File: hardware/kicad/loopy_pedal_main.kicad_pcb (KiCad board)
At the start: 2 copper layers, 82 x 94 mm, 84 parts, among them J1 USB, J10 MOCO, J11 IND, J12 UNDO, J13 MODE, J14 TRACK1, J15 TRACK2, J16 TRACK3, J17 TRACK4, J18 CLEAR, J19 BANK, J2 9V, J3 RECPLAY, J4 STOP, J5 RING, J6 ICSP U1, J7 ICSP U2, J8 MIDI OUT, J9 MIDI IN, Q1 AO3401A, SW1 RST U1, SW2 RST U2, U1 ATmega328P-A, U10 74AHCT1G08, U2 ATmega16U2-A, U3 AP63203WU, U4 74AHCT1G125, U5 LM66100DCK, U6 LM66100DCK, U7 USBLC6-2SC6, U8 74AHCT1G125, U9 H11L1, Y1 16MHz, Y2 16MHz

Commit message: fix(pcb): correct reverse-polarity FET, LM66100 footprint, ISP caps, TVS
Fixes all issues found during circuit validation + the assembled-board quote:

- Q1 (reverse-polarity P-FET): swap Source/Drain so Drain=input, Source=load,
  Gate=GND. The body diode now blocks reverse polarity instead of conducting
  it straight to the board. Normal operation unchanged.
- U5/U6 (LM66100 ideal diodes): footprint SOT-23-6 -> SOT-363_SC-70-6 (the
  LM66100DCK is an SC-70-6 part; the old footprint would not have fit).
- CLEAR (PB3/MOSI) + BANK (PB4/MISO) debounce caps: 100nF -> 1nF so the shared
  ICSP lines stay clean for in-system programming (firmware debounces anyway).
- D1: value TVS_SMBJ12A -> SMAJ12A to match the D_SMA footprint + the BOM part
  (Littelfuse SMAJ12A, 400W, C148213).

Rebuilt netlist -> board -> place -> route -> DRC: 969 segments, 67 vias,
2 GND pours, DRC 0 errors / 0 unconnected / 0 silk warnings.

Regenerated fab package (gerbers+drill, CPL, BOM) and JLCPCB upload files;
all 26 SMT BOM lines carry an in-stock LCSC part (new 1nF = C1588).

Co-Authored-By: Claude Opus 4.8 <noreply@anthropic.com>
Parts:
- C17, C18: value 100nF -> 1nF
- D1: value TVS_SMBJ12A -> SMAJ12A
- U5, U6: footprint SOT-23-6 -> SOT-363_SC-70-6
- moved C7 41.3 mm to (77.7, 92.8)
- moved C20 35.0 mm to (70.9, 96.9)
- moved C19 31.3 mm to (40.4, 90.1)
- moved C6 22.5 mm to (102.4, 81.4)
- moved C12 15.4 mm to (92.9, 95.4)
- moved C9 11.9 mm to (92.9, 97.8)
- moved U5 11.4 mm to (42.0, 84.9)
- moved C27 11.0 mm to (37.3, 85.0)
- moved Q1 9.98 mm to (37.0, 81.2)
- moved U6 9.43 mm to (45.8, 84.9)
- moved C25 9.34 mm to (49.6, 84.5)
- moved U4 9.03 mm to (50.0, 76.8)
- moved C8 8.77 mm to (85.2, 95.4)
- moved C15 8.21 mm to (85.2, 100.1)
- moved R14 8.21 mm to (48.1, 87.7)
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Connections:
- Q1 pad 2: VIN_RAW -> +9V
- Q1 pad 3: +9V -> VIN_RAW
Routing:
- net RING_DATA: track 53.9 -> 100.8 mm, vias 2 -> 0
- net GND: track 571.3 -> 607.2 mm, vias 4 -> 1
- net FB: track 49.4 -> 16.1 mm, vias 0 -> 2
- net N$16: track 37.4 -> 10.0 mm
- net SW_NODE: track 52.4 -> 26.5 mm, vias 0 -> 2
- net IND_DATA: track 62.8 -> 87.7 mm, vias 2 -> 0
- net N$21: track 71.0 -> 94.0 mm
- net SW_RECPLAY: track 77.7 -> 97.8 mm, vias 3 -> 2
- net +5V: track 250.0 -> 230.1 mm, vias 5 -> 9
- net SW_STOP: track 89.7 -> 70.3 mm
- net RST_16: track 40.5 -> 58.3 mm, vias 0 -> 1
- net RST_328: track 67.5 -> 51.3 mm
- net SW_MODE: track 60.0 -> 74.8 mm, vias 0 -> 2
- net N$8: track 78.4 -> 64.8 mm
- net N$3: track 44.2 -> 56.4 mm, vias 2 -> 3
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
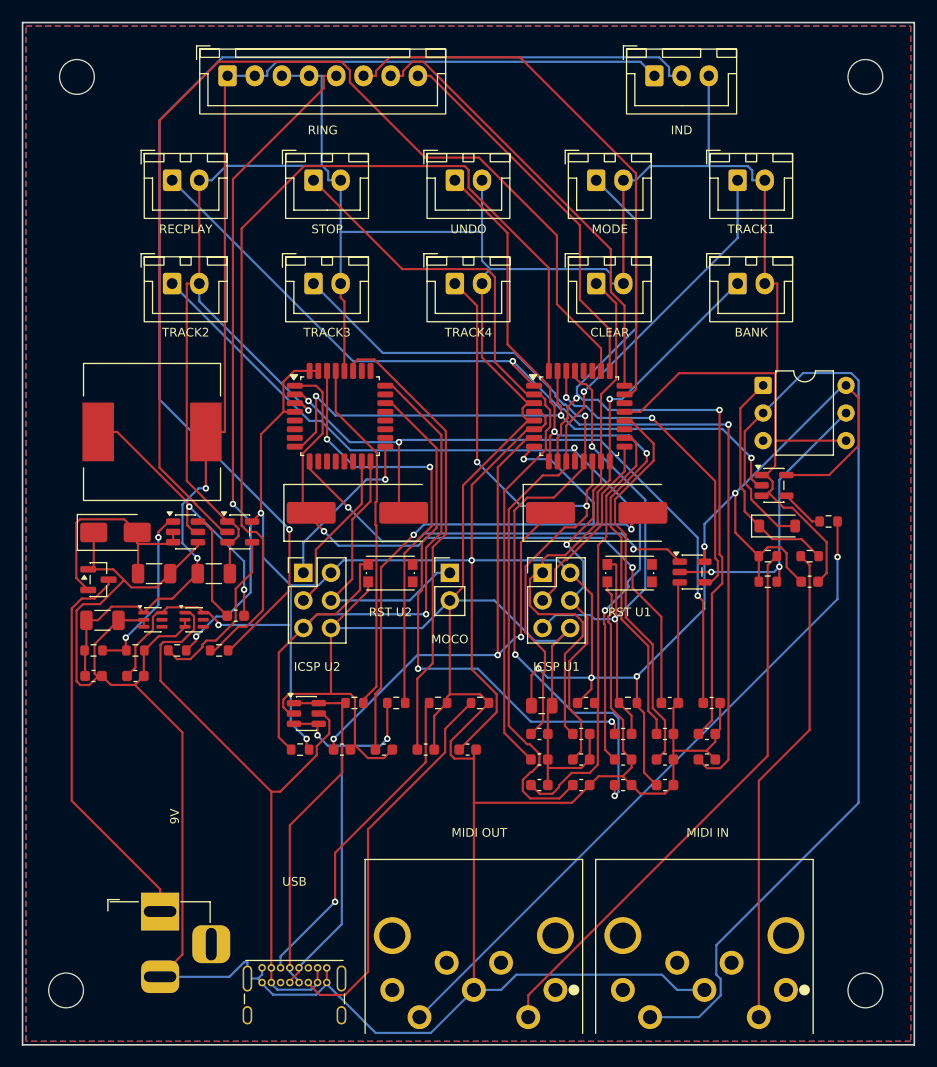
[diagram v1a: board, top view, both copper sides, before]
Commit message: fix(pcb): critical H11L1 MIDI-in bug + full placement/routing quality pass
From the 5-agent review:

CRITICAL fix:
- H11L1 opto (U9): pins 4/5 were swapped (datasheet: 4=Vo, 5=GND, 6=Vcc).
  As wired, the opto output was grounded and the "output" net was taken from
  the GND pin, killing ALL MIDI input (DIN + USB via the AND merge). Corrected.

Placement (guided clustering, was autorouter-scattered):
- Each crystal + its two 22pF load caps now placed as a tight triad at the MCU
  (~8mm, was ~20mm) -> reliable 16MHz startup, short oscillator loops.
- MCU VCC/AVCC/UCAP decoupling clustered at the IC pins.
- Buck: U3 + L1 compact (SW node 9.8mm) + input/output/BST caps clustered.

Routing/power:
- "Power" net-class: +9V / +5V_LED / VIN_RAW routed at 0.8mm (high-current
  rails; VBUS/+5V/SW_NODE kept default to fit fine-pitch fan-outs).
- 73 GND stitching vias tie the two ground pours together.
- HF 100nF input bypass added at the buck IN pin.

Rebuilt netlist -> place -> route -> finalize: DRC 0 errors / 0 unconnected /
0 warnings (980 segments, ~138 vias incl. stitching, 2 GND pours).
Regenerated fab package + JLCPCB upload files (26 SMT lines, all LCSC-filled).

Co-Authored-By: Claude Opus 4.8 <noreply@anthropic.com>
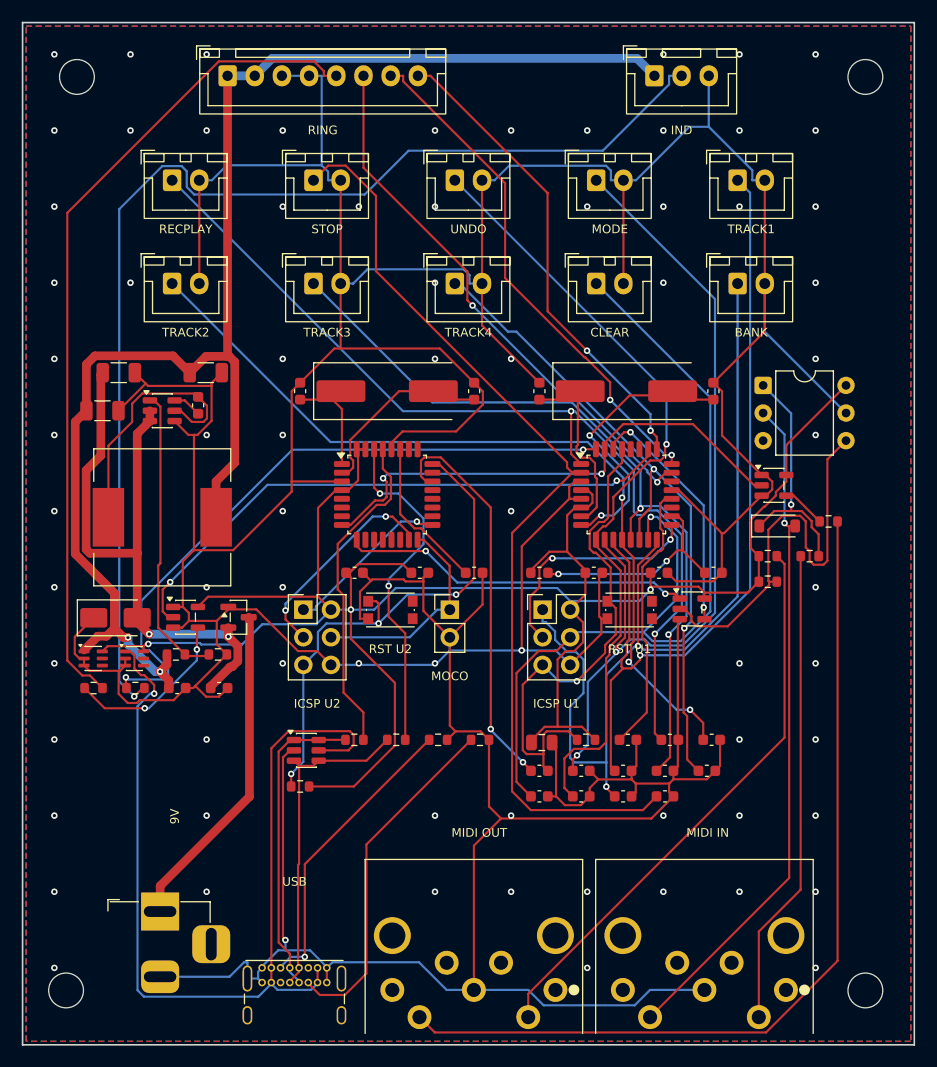
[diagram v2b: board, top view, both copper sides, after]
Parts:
- added C29: 100nF, C_0603_1608Metric, F.Cu at (48.1, 91.2)
- moved C4 44.8 mm to (93.5, 63.9), turned to 90 degrees
- moved C22 44.5 mm to (55.5, 63.9), turned to 90 degrees
- moved C3 37.6 mm to (77.5, 63.9), turned to 90 degrees
- moved C23 36.0 mm to (71.5, 63.9), turned to 90 degrees
- moved C1 25.2 mm to (93.5, 80.6)
- moved C19 22.3 mm to (60.5, 80.6)
- moved C5 20.6 mm to (82.5, 80.6)
- moved C25 19.7 mm to (46.1, 65.2), turned to 90 degrees
- moved C27 19.3 mm to (37.3, 65.7)
- moved C24 18.8 mm to (38.8, 62.2)
- moved C26 18.5 mm to (46.8, 62.2)
- moved C21 16.9 mm to (71.5, 80.6)
- moved C20 16.8 mm to (66.5, 80.6)
- moved C16 15.8 mm to (92.9, 98.8)
- moved C6 13.9 mm to (88.5, 80.6)
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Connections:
- U9 pad 4: GND -> MIDI_IN_OPTO
- U9 pad 5: MIDI_IN_OPTO -> GND
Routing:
- net N$7: track 61.1 -> 10.4 mm, vias 2 -> 0
- net N$8: track 64.8 -> 17.5 mm, vias 3 -> 0
- net RING_DATA: track 100.8 -> 53.5 mm, vias 0 -> 2
- net N$3: track 56.4 -> 17.3 mm, vias 3 -> 0
- net +5V: track 230.1 -> 192.1 mm, vias 9 -> 3
- net +9V: track 20.9 -> 57.6 mm, vias 0 -> 2
- net SW_CLEAR: track 49.6 -> 82.7 mm
- net N$21: track 94.0 -> 62.5 mm, vias 0 -> 1
- net SW_BANK: track 56.4 -> 86.0 mm, vias 1 -> 2
- net VBUS: track 57.9 -> 87.1 mm, vias 0 -> 1
- net N$4: track 55.4 -> 26.2 mm, vias 3 -> 2
- net +5V_LED: track 107.7 -> 136.6 mm
- net N$6: track 42.4 -> 14.2 mm
- net IND_DATA: track 87.7 -> 60.8 mm, vias 0 -> 2
- net N$17: track 61.5 -> 82.2 mm, vias 1 -> 0
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
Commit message: feat(pcb): add Q1 gate clamp, 16U2 AVCC filter, DIN shields to GND
Residual robustness items from the 5-agent review:

- Q1 reverse-polarity FET gate protection: 100k pull-down + 10V Zener (D3,
  BZT52C10) clamp gate-to-source, so an input transient (D1 clamps +9V to
  ~20V) can't drive Vgs past the AO3401's +/-12V limit.
- ATmega16U2 AVCC: now filtered from +5V via a ferrite (FB2) + 100nF, instead
  of being tied straight to +5V (matches the 328P's AVCC treatment).
- DIN-5 MIDI shield/earth tabs (J8/J9 footprint "G" pads, not in the symbol)
  tied to GND in the net importer for EMI/ESD + mechanical strength.

4 new parts (D3 Zener, FB2 ferrite, 100k, 100nF). Rebuilt netlist -> place ->
route -> finalize: DRC 0 errors / 0 unconnected / 0 warnings (949 segments,
148 vias incl. 81 GND stitching). Fab package + JLCPCB files regenerated;
all 28 SMT BOM lines LCSC-filled (100k C25803, Zener C216719).

Co-Authored-By: Claude Opus 4.8 <noreply@anthropic.com>
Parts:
- added C30: 100nF, C_0603_1608Metric, F.Cu at (59.4, 100.2)
- added D3: 10V, D_SOD-123, F.Cu at (37.4, 88.5)
- added FB2: FerriteBead, L_0603_1608Metric, F.Cu at (63.2, 100.2)
- added R15: 100k, R_0603_1608Metric, F.Cu at (36.5, 93.6)
- moved C29 21.0 mm to (67.1, 100.2)
- moved C9 12.3 mm to (77.5, 98.8)
- moved R8 11.9 mm to (36.5, 91.3)
- moved C8 8.05 mm to (85.2, 101.2)
- moved C10 7.70 mm to (81.4, 101.2)
- moved C12 7.70 mm to (89.1, 98.8)
- moved R7 5.59 mm to (49.7, 88.1)
- moved U5 5.59 mm to (42.1, 88.5)
- moved U6 5.59 mm to (45.9, 88.5)
- moved C28 3.85 mm to (48.1, 91.3)
- moved R14 3.85 mm to (44.2, 91.3)
- moved R9 3.85 mm to (40.4, 91.3)
- moved C18 3.85 mm to (89.1, 101.2)
- moved C13 2.88 mm to (85.7, 96.0)
- moved C2 2.88 mm to (85.2, 98.8)
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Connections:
- J8 pad G: (no net) -> GND
- J9 pad G: (no net) -> GND
- Q1 pad 1: GND -> Q1_GATE
- U2 pad 32: +5V -> AVCC16
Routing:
- net Q1_GATE: track 0.00 -> 79.0 mm
- net AVCC16: track 0.00 -> 43.0 mm, vias 0 -> 2
- net UART_RX: track 22.6 -> 64.1 mm
- net VBUS: track 87.1 -> 47.0 mm, vias 1 -> 2
- net SW_CLEAR: track 82.7 -> 60.7 mm, vias 1 -> 3
- net FB: track 27.4 -> 49.3 mm, vias 0 -> 3
- net RST_328: track 47.2 -> 64.3 mm, vias 1 -> 3
- net +9V: track 57.6 -> 74.4 mm, vias 2 -> 3
- net SW_MODE: track 79.4 -> 63.5 mm, vias 2 -> 1
- net +5V: track 192.1 -> 177.6 mm, vias 3 -> 4
- net SW_BANK: track 86.0 -> 72.6 mm, vias 2 -> 3
- net +5V_LED: track 136.6 -> 123.6 mm, vias 2 -> 0
- net N$20: track 21.9 -> 34.1 mm, vias 1 -> 0
- net SW_STOP: track 87.3 -> 75.1 mm, vias 0 -> 1
- net SW_TRACK1: track 75.9 -> 63.9 mm, vias 1 -> 2
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
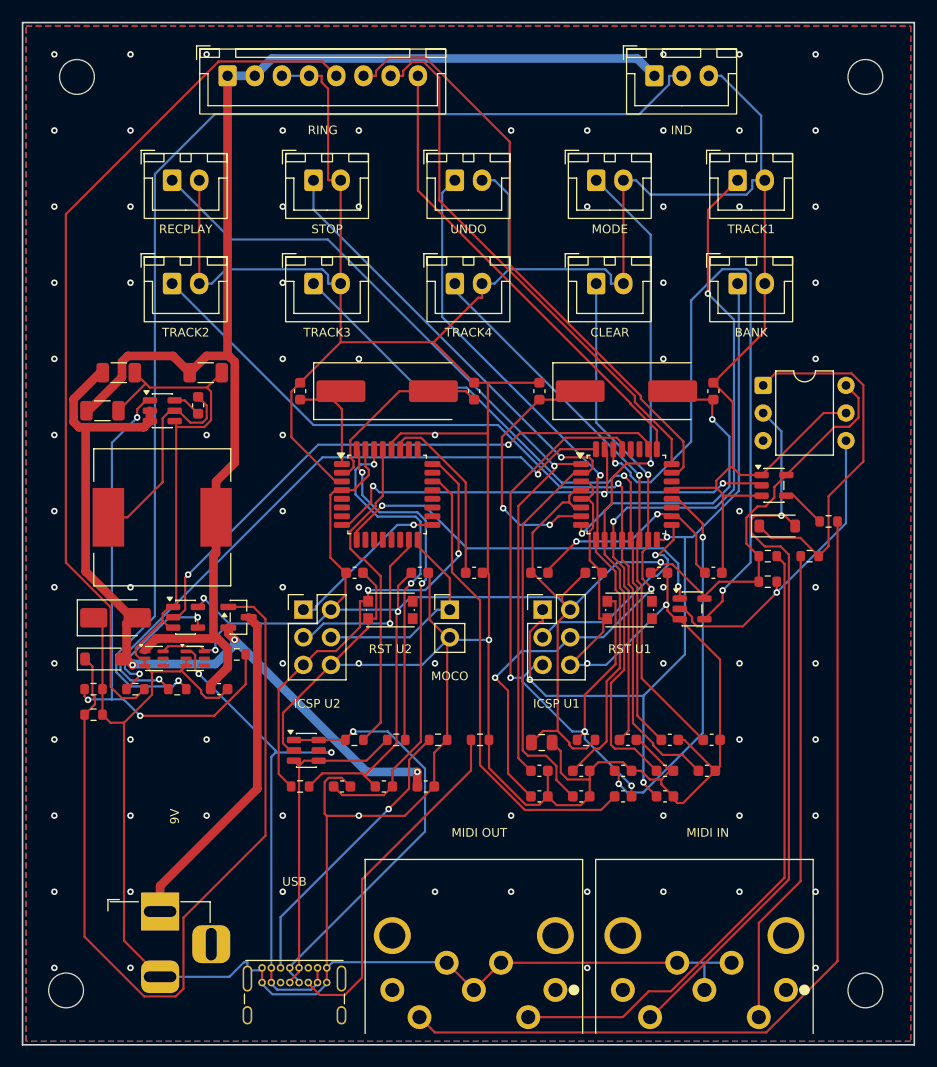
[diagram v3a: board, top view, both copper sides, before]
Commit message: fix(pcb): re-review fixes — reversed diodes, USB/DIN shields, buck cap
Second 5-agent review (post placement-pass) caught regressions the first
review and my own validation missed:

CRITICAL (board-dead, now fixed):
- D1 SMAJ12A TVS was reversed (KiCad Device:D pin1=cathode): cathode was on
  GND, anode on +9V -> forward-conducts and crowbars the +9V rail. Now
  cathode->+9V, anode->GND. (Latent since the original design.)
- D3 gate-clamp Zener was reversed -> forward-conducts and starves the Q1 gate
  so the reverse-polarity FET never turns on. Now cathode->+9V, anode->gate.

IMPORTANT:
- USB-C: all 4 shell/shield (SH) pads now tied to GND (was only 1).
- DIN-5 shield tabs grounded in the net importer (robust across rebuilds).
- Buck HF input cap (C29) pulled into the buck cluster at the IN pin (was
  auto-placed 41mm away, doing nothing).
- GND stitching: finalize now drops any via the fill leaves isolated.

Verified DRC 0 errors / 0 unconnected / 0 warnings (1047 segments, ~139 vias).
Fab package + JLCPCB files regenerated; 28/28 SMT lines LCSC-filled.

Known residual (not a functional blocker): crystal-to-MCU XTAL traces are
longish because the HC-49 sits opposite the XTAL pins; proper fix is relocating
the crystal to the pin edge or moving to a 3225 part. 16MHz is reliable at this
length in practice.

Co-Authored-By: Claude Opus 4.8 <noreply@anthropic.com>
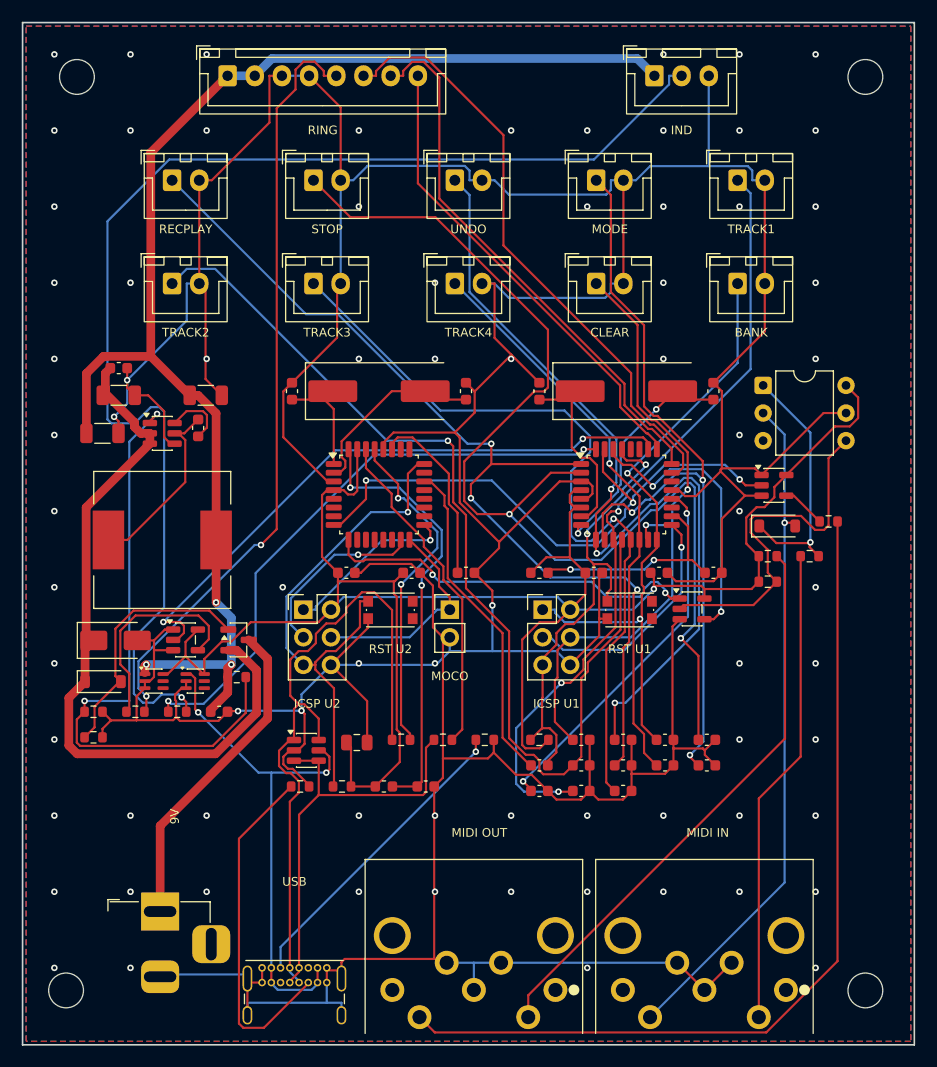
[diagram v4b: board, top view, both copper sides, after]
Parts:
- moved C29 47.7 mm to (38.8, 61.8)
- moved R6 17.1 mm to (55.5, 100.2)
- moved C7 17.0 mm to (60.7, 96.2)
- moved C10 12.7 mm to (92.9, 96.0)
- moved C14 11.6 mm to (81.4, 98.3)
- moved C9 11.6 mm to (89.1, 98.3)
- moved C16 8.47 mm to (85.2, 98.3)
- moved C8 8.21 mm to (77.5, 98.3)
- moved C2 7.92 mm to (77.5, 100.7)
- moved C30 7.70 mm to (67.1, 100.2)
- moved C17 6.47 mm to (81.4, 96.0)
- moved C13 6.36 mm to (81.4, 100.7)
- moved C15 6.36 mm to (85.2, 100.7)
- moved C18 5.20 mm to (89.1, 96.0)
- moved C11 4.79 mm to (85.2, 96.0)
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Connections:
- D1 pad 1: GND -> +9V
- D1 pad 2: +9V -> GND
- D3 pad 1: Q1_GATE -> +9V
- D3 pad 2: +9V -> Q1_GATE
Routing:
- net Q1_GATE: track 79.0 -> 23.4 mm
- net UART_RX: track 64.1 -> 26.2 mm
- net SW_STOP: track 75.1 -> 105.8 mm, vias 1 -> 2
- net GND: track 616.7 -> 592.2 mm, vias 83 -> 77
- net USB_D+: track 39.0 -> 62.4 mm, vias 1 -> 0
- net RST_328: track 64.3 -> 43.6 mm, vias 3 -> 2
- net SW_UNDO: track 63.9 -> 81.0 mm, vias 1 -> 3
- net SW_BANK: track 72.6 -> 58.5 mm, vias 3 -> 2
- net SW_TRACK2: track 79.5 -> 92.9 mm
- net DTR: track 42.8 -> 30.5 mm
- net SW_TRACK3: track 62.1 -> 73.2 mm
- net N$20: track 34.1 -> 23.1 mm, vias 0 -> 1
- net SW_RECPLAY: track 78.5 -> 89.4 mm, vias 1 -> 3
- net RING_DATA_OUT: track 80.3 -> 70.6 mm, vias 0 -> 2
- net SW_MODE: track 63.5 -> 73.0 mm, vias 1 -> 3
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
